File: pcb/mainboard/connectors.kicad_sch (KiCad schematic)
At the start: 52 parts, among them J28 SMPM, J29 SMPM, J30 SMPM, J31 SMPM, J32 SMPM, J33 SMPM, J34 SMPM, J35 SMPM, J36 SMPM, J37 SMPM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

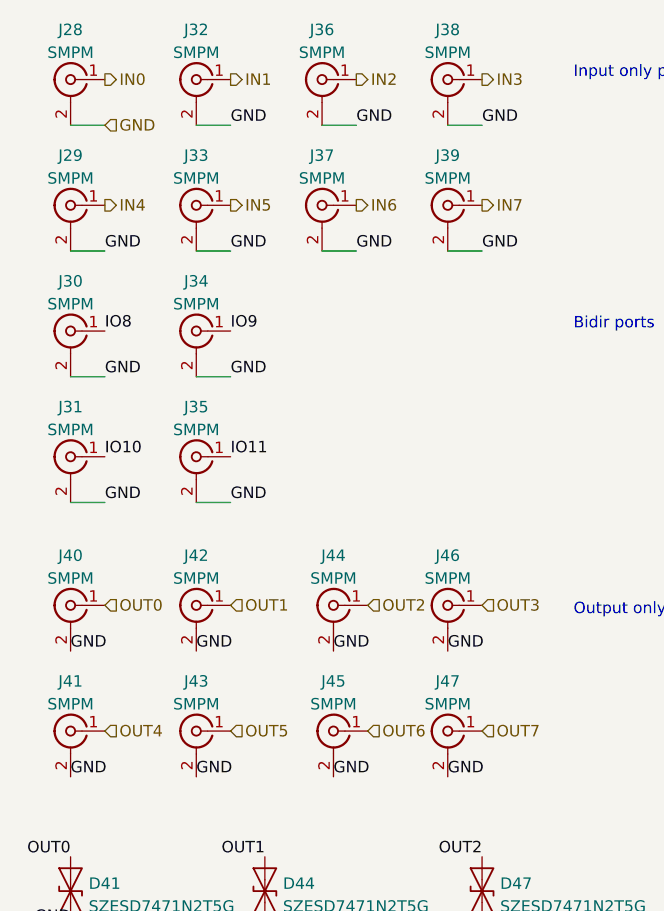
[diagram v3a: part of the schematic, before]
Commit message: Updated schematic with some notes on rework
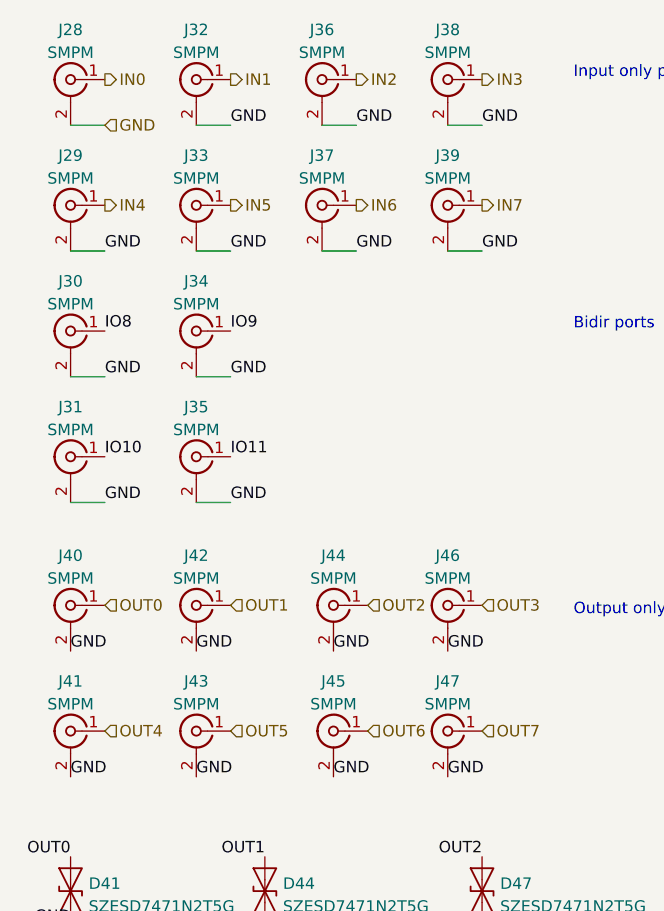
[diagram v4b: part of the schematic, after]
